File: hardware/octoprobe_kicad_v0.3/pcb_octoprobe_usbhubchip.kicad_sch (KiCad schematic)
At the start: 33 parts, among them J801 USB_C_Receptacle_USB2.0, U801 AMS1117-3.3, U802 USB2514B_Bi, Y801 24MHz

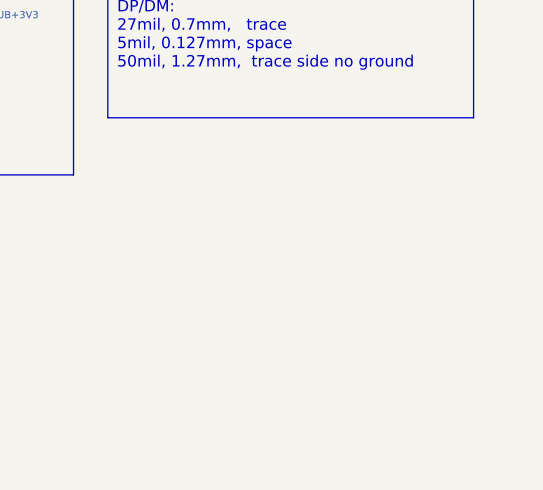
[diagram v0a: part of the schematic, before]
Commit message: PCB: Add "Open Hardware"
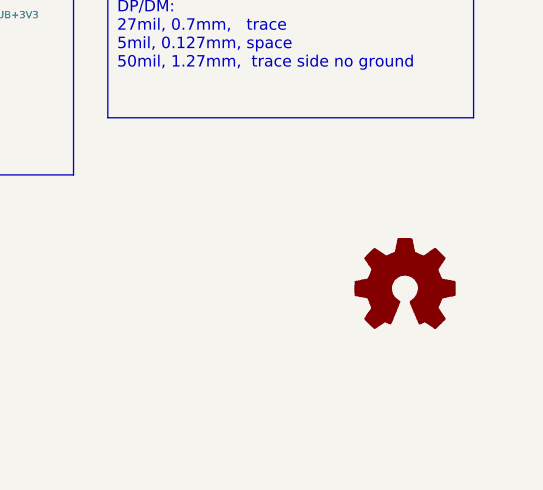
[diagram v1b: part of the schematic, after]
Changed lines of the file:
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@@
+	)
+	(symbol
+		(lib_id "Graphic:Logo_Open_Hardware_Small")
+		(at 275.59 173.99 0)
+		(unit 1)
+		(exclude_from_sim yes)
+		(in_bom no)
+		(on_board no)
+		(dnp no)
+		(fields_autoplaced yes)
+		(property "Reference" "#SYM301"
+			(at 275.59 167.005 0)
+			(effects
+				(font
+					(size 1.27 1.27)
+				)
+				(hide yes)
+			)
+		)
+		(property "Value" "Logo_Open_Hardware_Small"
+			(at 275.59 179.705 0)
+			(effects
+				(font
+					(size 1.27 1.27)
+				)
+				(hide yes)
+			)
+		)
+		(property "Footprint" ""
+			(at 275.59 173.99 0)
+			(effects
+				(font
+					(size 1.27 1.27)
+				)
+				(hide yes)
+			)
+		)
+		(property "Datasheet" "~"
+			(at 275.59 173.99 0)
+			(effects
+				(font
+					(size 1.27 1.27)
+				)
+				(hide yes)
+			)
+		)
+		(property "Description" "Open Hardware logo, small"
+			(at 275.59 173.99 0)
+			(effects
+				(font
+					(size 1.27 1.27)
+				)
+				(hide yes)
+			)
+		)
+		(instances
+			(project "pcb_octoprobe"
+				(path "/35c47459-45a7-4753-acae-c8b47e7575e1/cff48fa5-514e-40a1-9e85-b0c2e53fd5a3"
+					(reference "#SYM301")
+					(unit 1)
+				)
+			)
+		)
 	)
 	(symbol

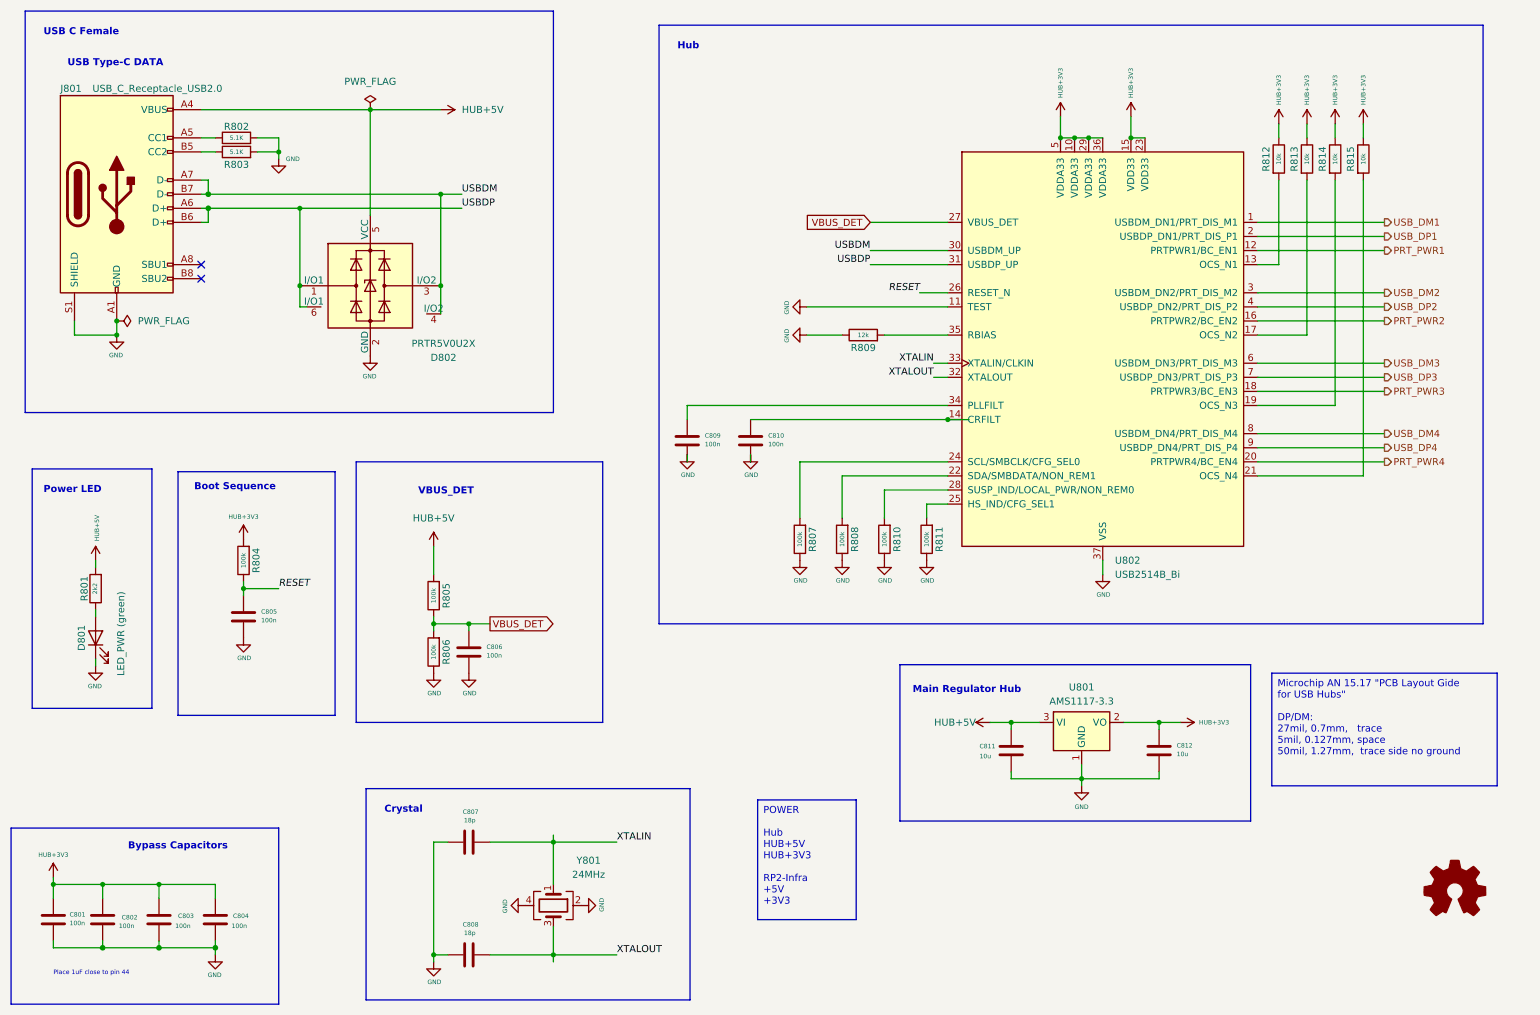
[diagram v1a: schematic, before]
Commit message: PCB: Production files ready
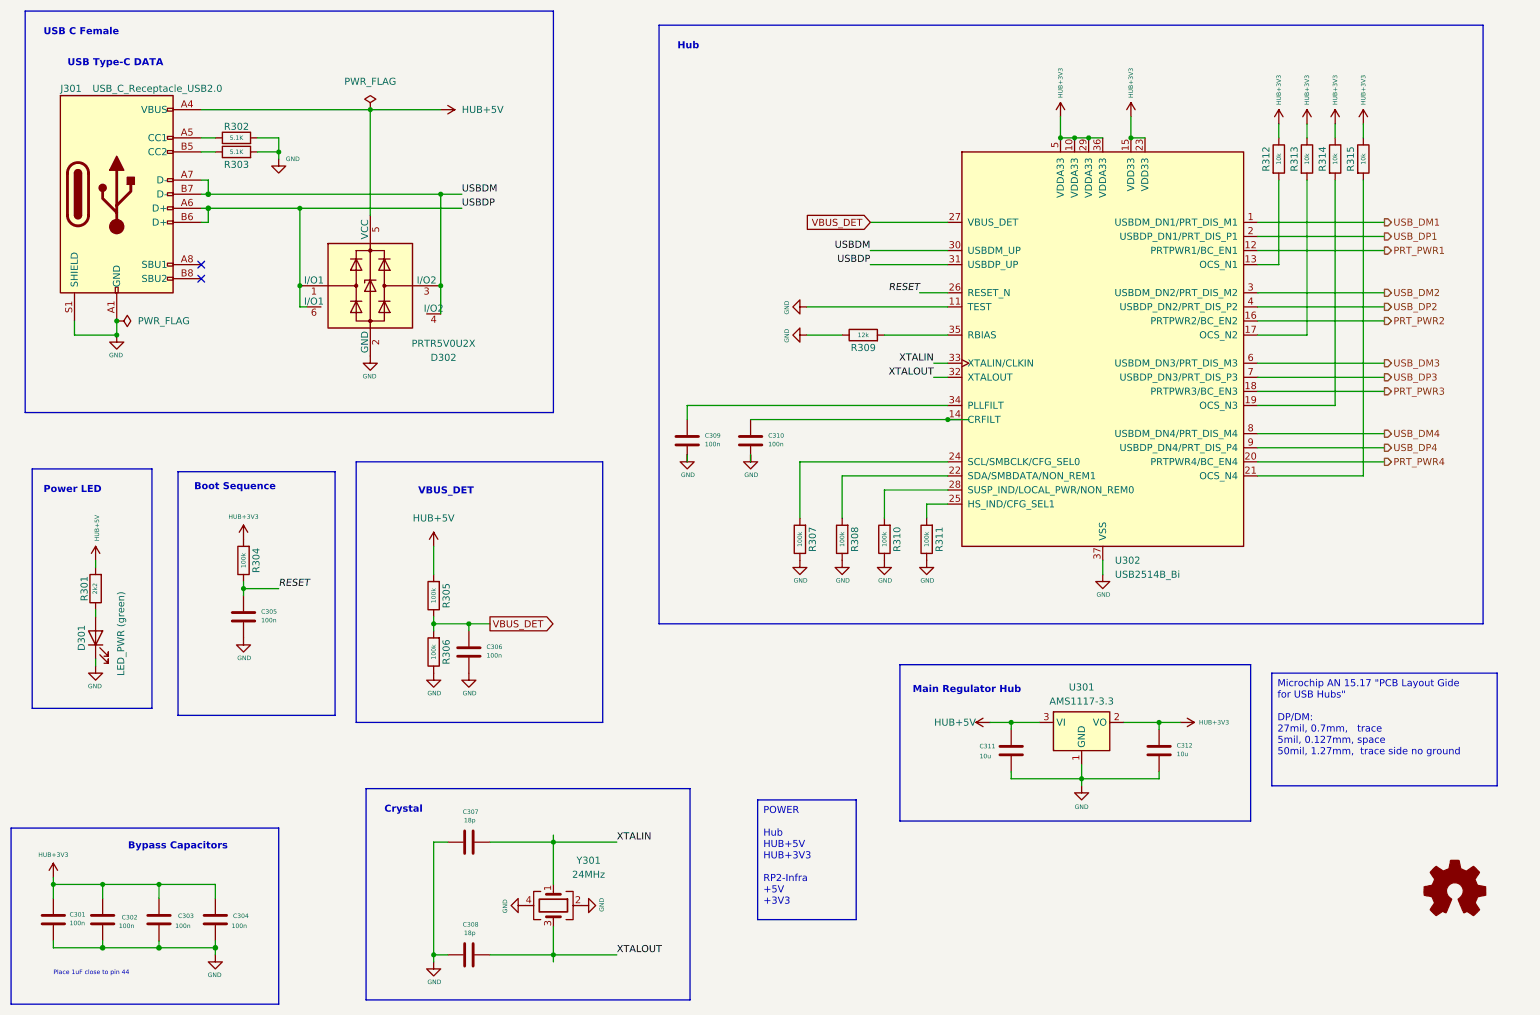
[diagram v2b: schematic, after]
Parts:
- D301: renamed from D801; footprint 00_project_library:LED_0603_1608Metric -> LED_SMD:LED_0805_2012Metric
- renumbered C801 to C301, C802 to C302, C803 to C303, C804 to C304, C805 to C305, C806 to C306, C807 to C307, C808 to C308, C809 to C309, C810 to C310, C811 to C311, C812 to C312, D802 to D302, J801 to J301, R801 to R301, R802 to R302, R803 to R303, R804 to R304, R805 to R305, R806 to R306, R807 to R307, R808 to R308, R809 to R309, R810 to R310, R811 to R311, R812 to R312, R813 to R313, R814 to R314, R815 to R315, U801 to U301, U802 to U302, Y801 to Y301
